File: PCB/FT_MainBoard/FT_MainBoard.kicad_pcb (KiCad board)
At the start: 2 copper layers, 34 parts

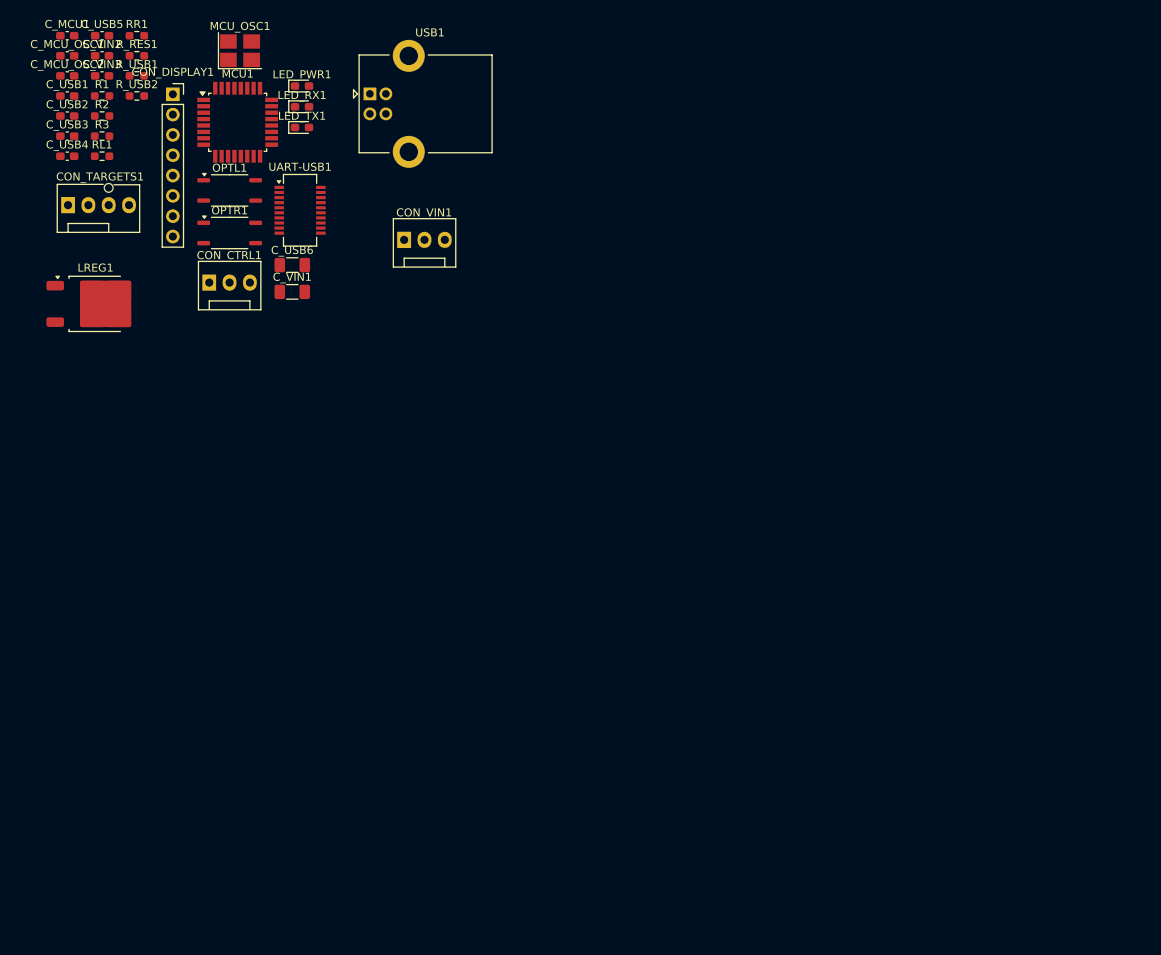
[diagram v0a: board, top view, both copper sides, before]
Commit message: create main board PCB
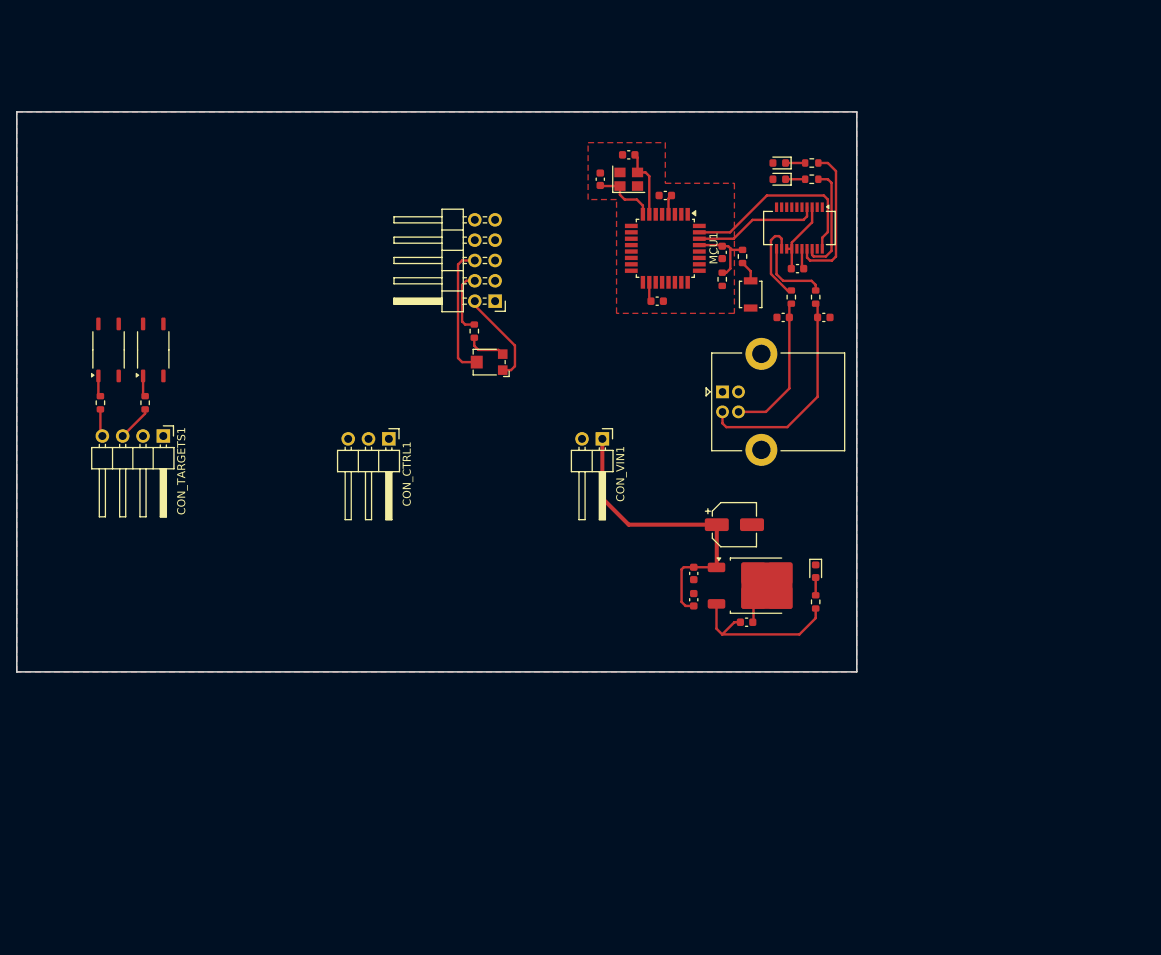
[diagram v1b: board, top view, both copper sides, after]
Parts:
- removed C_USB4: 1nF, Capacitor_SMD:C_0603_1608Metric_Pad1.08x0.95mm_HandSolder
- removed C_USB5: 100nF, Capacitor_SMD:C_0603_1608Metric_Pad1.08x0.95mm_HandSolder
- removed C_USB6: 100uF, Capacitor_SMD:C_1206_3216Metric_Pad1.33x1.80mm_HandSolder
- removed MCU_OSC1: 16MHz, Crystal:Crystal_SMD_3225-4Pin_3.2x2.5mm_HandSoldering
- added C_LREG1: 100nF, Capacitor_SMD:C_0603_1608Metric, F.Cu at (141.2, 113.8)
- added C_MCU2: 100nF, Capacitor_SMD:C_0603_1608Metric, F.Cu at (130.0, 73.7)
- added C_RES1: 100nF, Capacitor_SMD:C_0603_1608Metric, F.Cu at (138.2, 67.6)
- added OSC_MCU1: 16MHz, Crystal:Crystal_SMD_3225-4Pin_3.2x2.5mm, F.Cu at (126.5, 58.4)
- added RV_DISPLAY1: 10K, Potentiometer_SMD:Potentiometer_Bourns_TC33X_Vertical, F.Cu at (108.9, 81.3)
- added R_DISPLAY1: 220R, Resistor_SMD:R_0603_1608Metric, F.Cu at (107.2, 77.4)
- added R_RES2: 330R, Resistor_SMD:R_0603_1608Metric, F.Cu at (140.7, 68.1)
- added SW1: SW_Push, Button_Switch_SMD:SW_SPST_B3U-1000P, F.Cu at (141.7, 72.8)
- CON_CTRL1: footprint Connector:FanPinHeader_1x03_P2.54mm_Vertical -> Connector_PinHeader_2.54mm:PinHeader_1x03_P2.54mm_Horizontal
- CON_DISPLAY1: value Conn_01x08_Pin -> Conn_02x05_Odd_Even; footprint Connector_PinSocket_2.54mm:PinSocket_1x08_P2.54mm_Vertical -> Connector_PinHeader_2.54mm:PinHeader_2x05_P2.54mm_Horizontal
- CON_TARGETS1: footprint Connector:FanPinHeader_1x04_P2.54mm_Vertical -> Connector_PinHeader_2.54mm:PinHeader_1x04_P2.54mm_Horizontal
- CON_VIN1: value Conn_01x03_Pin -> Conn_01x02_Pin; footprint Connector:FanPinHeader_1x03_P2.54mm_Vertical -> Connector_PinHeader_2.54mm:PinHeader_1x02_P2.54mm_Horizontal
- C_MCU1, C_MCU_OSC1, C_MCU_OSC2, C_USB1, C_USB2, C_USB3, C_VIN2, C_VIN3: footprint Capacitor_SMD:C_0603_1608Metric_Pad1.08x0.95mm_HandSolder -> Capacitor_SMD:C_0603_1608Metric
- C_VIN1: footprint Capacitor_SMD:C_1206_3216Metric_Pad1.33x1.80mm_HandSolder -> Capacitor_SMD:CP_Elec_5x5.8
- LED_PWR1, LED_RX1, LED_TX1: footprint LED_SMD:LED_0603_1608Metric_Pad1.05x0.95mm_HandSolder -> LED_SMD:LED_0603_1608Metric
- R1, R2, R3, R_RES1, R_USB1, R_USB2: footprint Resistor_SMD:R_0603_1608Metric_Pad0.98x0.95mm_HandSolder -> Resistor_SMD:R_0603_1608Metric
- RL1, RR1: value 1K -> 500R; footprint Resistor_SMD:R_0603_1608Metric_Pad0.98x0.95mm_HandSolder -> Resistor_SMD:R_0603_1608Metric
- moved R1 109.3 mm to (149.9, 111.3), turned to 90 degrees
- moved C_VIN3 98.8 mm to (134.6, 111.0), turned to 90 degrees
- moved C_VIN2 98.3 mm to (134.6, 107.7), turned to -90 degrees
- moved C_USB2 97.9 mm to (150.9, 75.7), turned to 180 degrees
- moved C_USB1 93.8 mm to (147.6, 69.6), turned to 180 degrees
- moved C_USB3 92.3 mm to (145.8, 75.7)
- moved LREG1 89.9 mm to (142.5, 109.2)
- moved R_USB1 89.2 mm to (149.9, 73.2), turned to -90 degrees
- moved R2 89.1 mm to (149.4, 58.4)
- moved R3 88.8 mm to (149.4, 56.4)
- moved LED_PWR1 88.3 mm to (149.9, 107.4), turned to -90 degrees
- moved R_USB2 85.6 mm to (146.8, 73.2), turned to -90 degrees
- moved R_RES1 78.3 mm to (138.2, 70.9), turned to 90 degrees
- moved C_MCU1 77.4 mm to (131.1, 60.5), turned to 180 degrees
- moved C_MCU_OSC1 71.3 mm to (126.5, 55.4), turned to 180 degrees
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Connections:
- MCU1 pad 10: unconnected-(MCU1-PD6-Pad10) -> GND
- MCU1 pad 11: unconnected-(MCU1-PD7-Pad11) -> GND
- MCU1 pad 12: Net-(CON_DISPLAY1-Pin_8) -> Net-(CON_DISPLAY1-Pin_3)
- MCU1 pad 13: Net-(CON_DISPLAY1-Pin_7) -> Net-(CON_DISPLAY1-Pin_5)
- MCU1 pad 14: Net-(CON_DISPLAY1-Pin_6) -> Net-(CON_DISPLAY1-Pin_7)
- MCU1 pad 15: Net-(CON_DISPLAY1-Pin_5) -> Net-(CON_DISPLAY1-Pin_9)
- MCU1 pad 16: Net-(CON_DISPLAY1-Pin_4) -> Net-(CON_DISPLAY1-Pin_10)
- MCU1 pad 17: Net-(CON_DISPLAY1-Pin_3) -> Net-(CON_DISPLAY1-Pin_8)
- MCU1 pad 20: unconnected-(MCU1-AREF-Pad20) -> GND
- MCU1 pad 23: unconnected-(MCU1-PC0-Pad23) -> GND
- MCU1 pad 24: unconnected-(MCU1-PC1-Pad24) -> GND
- MCU1 pad 25: unconnected-(MCU1-PC2-Pad25) -> GND
- MCU1 pad 26: unconnected-(MCU1-PC3-Pad26) -> GND
- MCU1 pad 27: unconnected-(MCU1-PC4-Pad27) -> GND
- MCU1 pad 28: unconnected-(MCU1-PC5-Pad28) -> GND
- MCU1 pad 29: Net-(MCU1-~{RESET}/PC6) -> RES
- R_RES1 pad 1: Net-(MCU1-~{RESET}/PC6) -> +5V
- R_RES1 pad 2: +5V -> RES
- USB1 pad 1: +5V -> unconnected-(USB1-VBUS-Pad1)
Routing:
- net +12V: track 0.00 -> 38.7 mm
- net +5V: track 0.00 -> 30.7 mm
- net /USB_D-: track 0.00 -> 26.8 mm
- net /TXD: track 0.00 -> 24.6 mm
- net Net-(UART-USB1-CBUS1): track 0.00 -> 18.4 mm
- net /USB_D+: track 0.00 -> 18.3 mm
- net GND: track 0.00 -> 17.9 mm
- net Net-(CON_DISPLAY1-Pin_6): track 0.00 -> 16.5 mm
- net /RXD: track 0.00 -> 15.8 mm
- net Net-(UART-USB1-CBUS0): track 0.00 -> 13.9 mm
- net Net-(UART-USB1-USBDM): track 0.00 -> 10.6 mm
- net RES: track 0.00 -> 9.41 mm
- net Net-(UART-USB1-3V3OUT): track 0.00 -> 9.39 mm
- net Net-(UART-USB1-USBDP): track 0.00 -> 9.32 mm
- net Net-(MCU1-XTAL1/PB6): track 0.00 -> 8.77 mm
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- added copper zone on B.Cu, net GND
- added copper zone on F.Cu, net GND
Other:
- board outline added: 105 x 70 mm

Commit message: update pcbs
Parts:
- moved CON_DISPLAY1 9.10 mm to (118.9, 73.2)
- moved RV_DISPLAY1 9.10 mm to (118.0, 80.8)
- moved R_DISPLAY1 9.10 mm to (116.3, 76.9)
- moved LED_PWR1 1.02 mm to (148.8, 107.4)
- moved R1 1.02 mm to (148.8, 111.3)
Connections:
- CON_DISPLAY1 pad 10: Net-(CON_DISPLAY1-Pin_10) -> DISPLAY_EN
- CON_DISPLAY1 pad 3: Net-(CON_DISPLAY1-Pin_3) -> DISPLAY_D0
- CON_DISPLAY1 pad 5: Net-(CON_DISPLAY1-Pin_5) -> DISPLAY_D1
- CON_DISPLAY1 pad 7: Net-(CON_DISPLAY1-Pin_7) -> DISPLAY_D2
- CON_DISPLAY1 pad 8: Net-(CON_DISPLAY1-Pin_8) -> DISPLAY_RS
- CON_DISPLAY1 pad 9: Net-(CON_DISPLAY1-Pin_9) -> DISPLAY_D3
- MCU1 pad 12: Net-(CON_DISPLAY1-Pin_3) -> DISPLAY_RS
- MCU1 pad 13: Net-(CON_DISPLAY1-Pin_5) -> DISPLAY_EN
- MCU1 pad 14: Net-(CON_DISPLAY1-Pin_7) -> DISPLAY_D3
- MCU1 pad 15: Net-(CON_DISPLAY1-Pin_9) -> DISPLAY_D2
- MCU1 pad 16: Net-(CON_DISPLAY1-Pin_10) -> DISPLAY_D1
- MCU1 pad 17: Net-(CON_DISPLAY1-Pin_8) -> DISPLAY_D0
- MCU1 pad 19: unconnected-(MCU1-PE2-Pad19) -> GND
- MCU1 pad 22: unconnected-(MCU1-PE3-Pad22) -> GND
- MCU1 pad 3: unconnected-(MCU1-PE0-Pad3) -> GND
- MCU1 pad 6: unconnected-(MCU1-PE1-Pad6) -> GND
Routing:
- net +5V: track 30.7 -> 155.3 mm
- net +12V: track 38.7 -> 108.4 mm
- net DISPLAY_RS: track 0.00 -> 20.3 mm
- net DISPLAY_EN: track 0.00 -> 14.2 mm
- net DISPLAY_D0: track 0.00 -> 12.1 mm
- net DISPLAY_D3: track 0.00 -> 10.1 mm
- net DISPLAY_D2: track 0.00 -> 9.40 mm
- net DISPLAY_D1: track 0.00 -> 8.68 mm
- net GND: track 17.9 -> 21.6 mm
- net Net-(CON_DISPLAY1-Pin_4): track 8.05 -> 7.33 mm

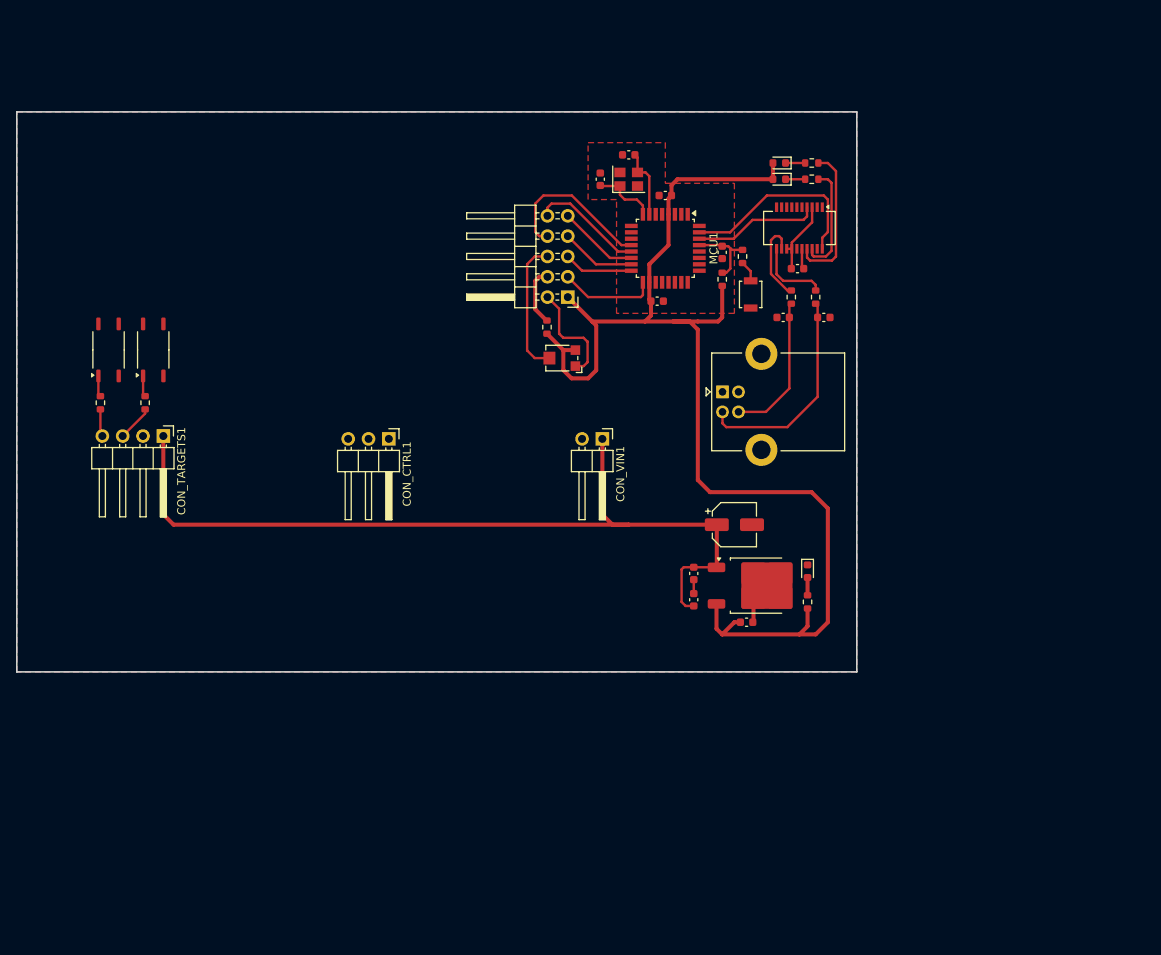
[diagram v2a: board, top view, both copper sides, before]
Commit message: hall and switch done
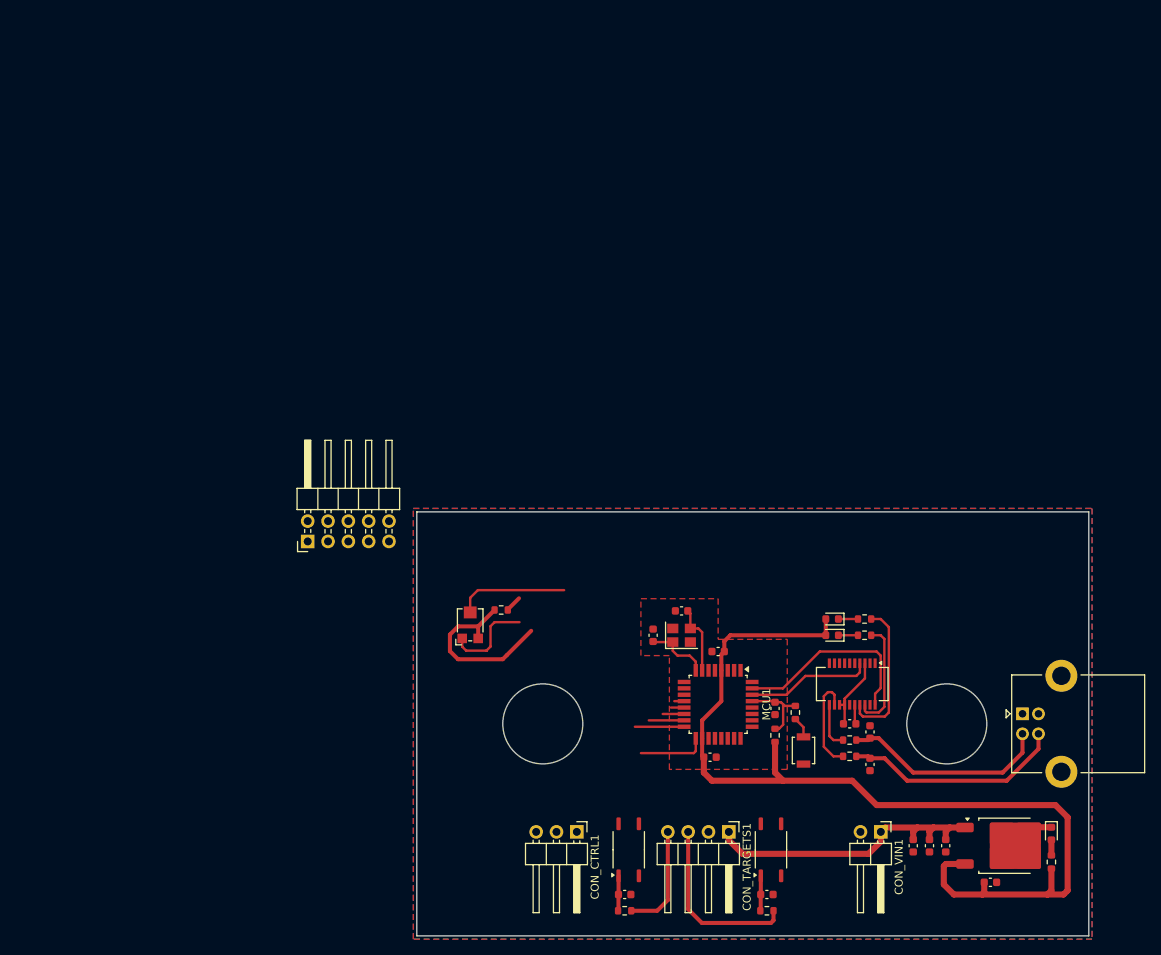
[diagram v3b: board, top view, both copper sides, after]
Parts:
- added C_OPTL1: 5nF, Capacitor_SMD:C_0603_1608Metric, F.Cu at (143.8, 147.8)
- added C_OPTR1: 5nF, Capacitor_SMD:C_0603_1608Metric, F.Cu at (126.0, 147.8)
- C_VIN1: value 100uF -> 1uF; footprint Capacitor_SMD:CP_Elec_5x5.8 -> Capacitor_SMD:C_0603_1608Metric
- RL1, RR1: value 500R -> 550R
- moved RL1 100.4 mm to (143.8, 149.9), turned to 0 degrees
- moved OPTL1 99.3 mm to (144.3, 142.2)
- moved RR1 91.3 mm to (126.0, 149.9), turned to 0 degrees
- moved OPTR1 90.2 mm to (126.5, 142.2)
- moved CON_TARGETS1 86.3 mm to (139.0, 140.0)
- moved CON_VIN1 60.2 mm to (158.0, 140.0)
- moved R_USB2 57.9 mm to (154.1, 130.6), turned to 0 degrees
- moved SW1 57.4 mm to (148.3, 129.8)
- moved C_MCU1 57.4 mm to (137.7, 117.5)
- moved C_RES1 57.4 mm to (144.8, 124.6)
- moved LED_TX1 57.4 mm to (151.9, 115.4)
- moved MCU1 57.4 mm to (137.7, 124.1)
- moved R2 57.4 mm to (156.0, 115.4)
- moved R_RES1 57.4 mm to (144.8, 127.9)
- moved LED_RX1 57.4 mm to (151.9, 113.4)
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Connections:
- R2 pad 2: Net-(UART-USB1-CBUS0) -> Net-(UART-USB1-CBUS2)
- UART-USB1 pad 10: unconnected-(UART-USB1-CBUS2-Pad10) -> Net-(UART-USB1-CBUS2)
- UART-USB1 pad 18: Net-(UART-USB1-CBUS0) -> unconnected-(UART-USB1-CBUS0-Pad18)
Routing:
- net +12V: track 108.4 -> 38.5 mm
- net DISPLAY_RS: track 20.3 -> 1.23 mm
- net /LEFT: track 4.50 -> 22.4 mm
- net (no net): track 0.00 -> 13.9 mm
- net Net-(UART-USB1-CBUS0): track 13.9 -> 0.00 mm
- net DISPLAY_EN: track 14.2 -> 1.65 mm
- net +5V: track 155.3 -> 143.7 mm
- net /RIGHT: track 3.44 -> 13.7 mm
- net /USB_D+: track 18.3 -> 27.6 mm
- net DISPLAY_D3: track 10.1 -> 2.68 mm
- net Net-(CON_DISPLAY1-Pin_4): track 7.33 -> 2.04 mm
- net DISPLAY_D2: track 9.40 -> 4.42 mm
- net GND: track 21.6 -> 17.0 mm
- net DISPLAY_D0: track 12.1 -> 8.55 mm
- net Net-(UART-USB1-USBDP): track 9.32 -> 5.82 mm
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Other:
- board size 105 x 70 mm -> 84 x 53 mm

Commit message: main board update
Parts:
- removed CON_DISPLAY1: Conn_02x05_Odd_Even, Connector_PinHeader_2.54mm:PinHeader_2x05_P2.54mm_Horizontal
- removed RV_DISPLAY1: 10K, Potentiometer_SMD:Potentiometer_Bourns_TC33X_Vertical
- removed R_DISPLAY1: 220R, Resistor_SMD:R_0603_1608Metric
- added C_RES2: 100nF, Capacitor_SMD:C_0603_1608Metric, F.Cu at (149.9, 114.3)
- added SW2: SW_SPST, Button_Switch_THT:SW_DIP_SPSTx01_Slide_9.78x4.72mm_W7.62mm_P2.54mm, F.Cu at (146.3, 121.6)
- CON_CTRL1: value Conn_01x03_Pin -> Conn_01x04_Pin; footprint Connector_PinHeader_2.54mm:PinHeader_1x03_P2.54mm_Horizontal -> Connector_PinHeader_2.54mm:PinHeader_1x04_P2.54mm_Horizontal
- C_OPTL1, C_OPTR1: value 5nF -> 100nF
- R_RES1: value 4.7k -> 10K
- moved C_USB2 5.32 mm to (153.9, 132.1), turned to 180 degrees
- moved C_USB3 4.89 mm to (153.9, 127.5), turned to 180 degrees
- moved LED_RX1 2.98 mm to (152.4, 116.3)
- moved R_USB1 2.04 mm to (153.9, 130.6)
- moved LED_TX1 1.70 mm to (152.4, 113.8)
- moved R_USB2 1.54 mm to (153.9, 129.0)
- moved R_RES2 1.02 mm to (146.3, 125.0)
- moved R2 0.91 mm to (156.0, 116.3)
- moved C_RES1 0.65 mm to (144.3, 125.0)
- moved C_USB1 0.54 mm to (153.9, 126.0)
- moved R_RES1 0.51 mm to (144.3, 128.0)
- moved SW1 0.51 mm to (147.8, 129.8)
- moved R3 0.40 mm to (156.0, 113.8), turned to 180 degrees
- moved C_MCU2 0.11 mm to (136.7, 130.6)
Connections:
- net /LEFT renamed /IN_LEFT
- net /OPTL>MCU renamed OPTL
- net /OPTR>MCU renamed OPTR
- net /RIGHT renamed /IN_RIGHT
- net /START renamed START
- net /STOP/RES renamed STOP
- MCU1 pad 10: GND -> RESET
- MCU1 pad 30: /RXD -> MCU_RX
- MCU1 pad 31: /TXD -> MCU_TX
- R2 pad 1: Net-(LED_TX1-K) -> Net-(LED_RX1-K)
- R3 pad 1: Net-(LED_RX1-K) -> Net-(UART-USB1-CBUS1)
- R3 pad 2: Net-(UART-USB1-CBUS1) -> Net-(LED_TX1-K)
- UART-USB1 pad 1: unconnected-(UART-USB1-~{DTR}-Pad1) -> DTR
- UART-USB1 pad 20: /TXD -> MCU_RX
- UART-USB1 pad 4: /RXD -> MCU_TX
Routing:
- net /TXD: track 24.6 -> 0.00 mm
- net MCU_RX: track 0.00 -> 19.6 mm
- net MCU_TX: track 0.00 -> 16.0 mm
- net /RXD: track 15.8 -> 0.00 mm
- net Net-(CON_DISPLAY1-Pin_6): track 14.0 -> 0.00 mm
- net (no net): track 13.9 -> 0.00 mm
- net DTR: track 0.00 -> 12.1 mm
- net GND: track 17.0 -> 7.53 mm
- net DISPLAY_D0: track 8.55 -> 0.00 mm
- net Net-(UART-USB1-CBUS2): track 0.00 -> 7.37 mm
- net Net-(UART-USB1-3V3OUT): track 9.32 -> 2.63 mm
- net Net-(UART-USB1-USBDM): track 12.2 -> 5.69 mm
- net DISPLAY_D1: track 6.16 -> 0.00 mm
- net DISPLAY_D2: track 4.42 -> 0.00 mm
- net Net-(SW2-B): track 0.00 -> 3.57 mm
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
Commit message: main board update
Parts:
- added C_IN1: 100n, Capacitor_SMD:C_0603_1608Metric, F.Cu at (81.5, 122.7)
- added C_IN2: 100n, Capacitor_SMD:C_0603_1608Metric, F.Cu at (81.5, 125.2)
- added C_IN3: 100n, Capacitor_SMD:C_0603_1608Metric, F.Cu at (81.5, 127.7)
- added R_IN1: 1000R, Resistor_SMD:R_0603_1608Metric, F.Cu at (81.5, 130.2)
- added R_IN2: 1000R, Resistor_SMD:R_0603_1608Metric, F.Cu at (81.5, 132.7)
- added R_IN3: 1000R, Resistor_SMD:R_0603_1608Metric, F.Cu at (81.5, 135.2)
- added R_IN4: 1000R, Resistor_SMD:R_0603_1608Metric, F.Cu at (81.5, 137.7)
- added R_IN5: 1000R, Resistor_SMD:R_0603_1608Metric, F.Cu at (81.5, 140.2)
- added R_IN6: 1000R, Resistor_SMD:R_0603_1608Metric, F.Cu at (81.5, 142.7)
- added SCH1: 74HC3G14DP,125, Package_SO:MSOP-8_3x3mm_P0.65mm, F.Cu at (105.1, 115.4)
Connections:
- CON_CTRL1 pad 2: START -> Net-(CON_CTRL1-Pin_2)
- CON_CTRL1 pad 3: STOP -> Net-(CON_CTRL1-Pin_3)
- CON_CTRL1 pad 4: RESET -> Net-(CON_CTRL1-Pin_4)
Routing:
- net Net-(UART-USB1-3V3OUT): track 2.63 -> 8.87 mm, vias 0 -> 2
